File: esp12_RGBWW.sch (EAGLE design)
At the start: 29 parts

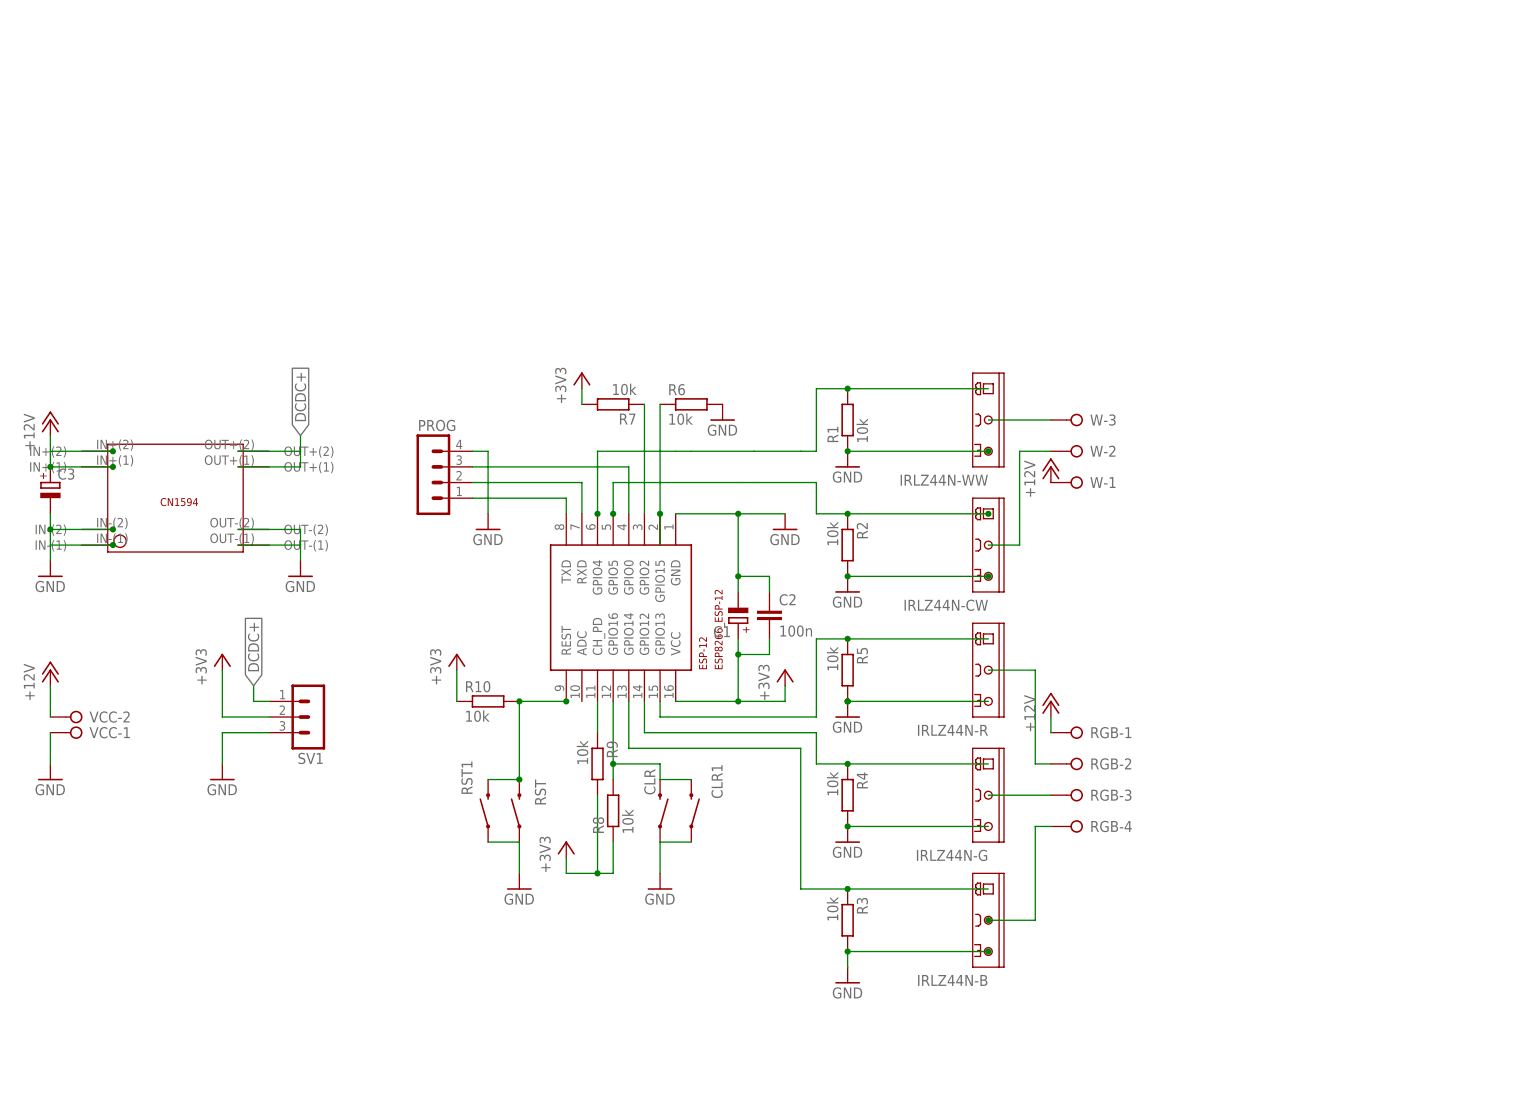
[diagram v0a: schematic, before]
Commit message: new, smaller board
new design, integrated DCDC converter, new, smaller MOSFETs, smaller overal board, additional PRG button, mostly optimized for SMD manufacturing but still hand solderable
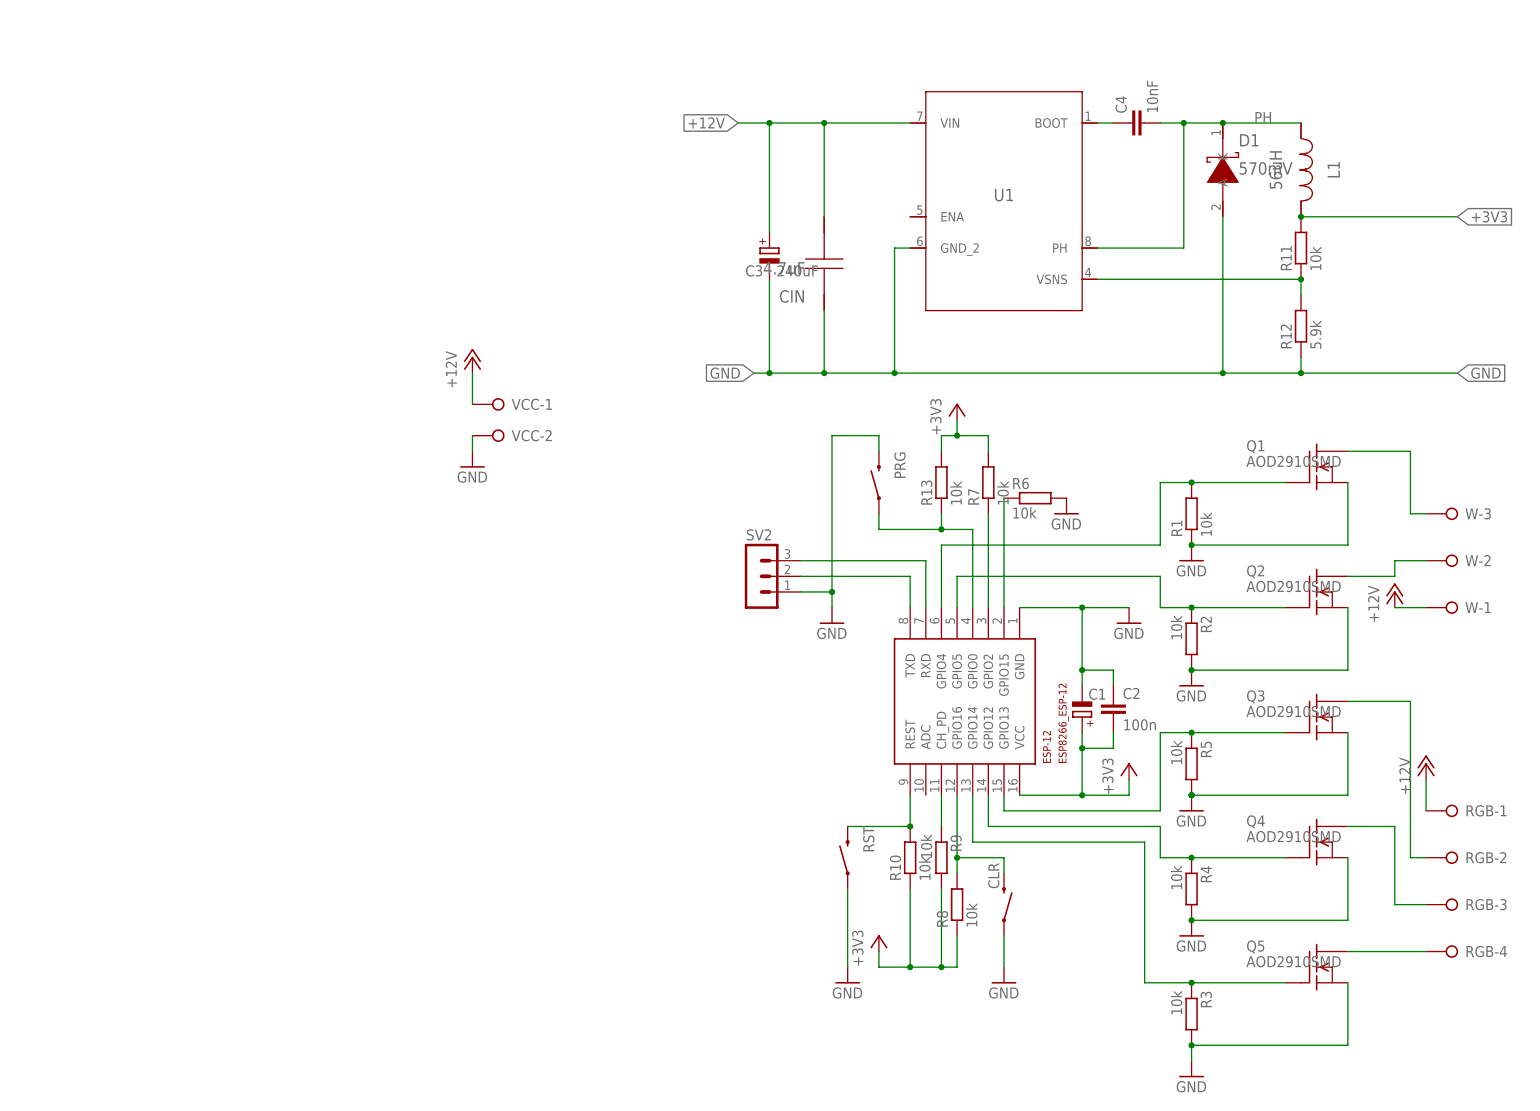
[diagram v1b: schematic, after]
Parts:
- removed CLR1, RST1: SWITCH-MOMENTARY-2SMD-1101NE, SparkFun-Electromechanical:SWITCH-MOMENTARY-2SMD-1101NE
- removed IRLZ44N-B, IRLZ44N-CW, IRLZ44N-G, IRLZ44N-R, IRLZ44N-WW: TIP121, PAsystem:TIP121
- removed PROG: (no value), con-lstb:MA04-1
- removed SV1: (no value), con-lstb:MA03-1
- removed U$2: XM1584, XM1584:XM1584
- added C4: 10nF, resistor:C-EUC0805
- added CIN: 4.7uF, AcceleratedDesigns_Lib:GRM31CR71H475KA12L
- added D1: 570mV, AcceleratedDesigns_Lib:PMEG6010CEH,115
- added L1: 56uH, AcceleratedDesigns_Lib:NPI75C560KTRF
- added PRG: SWITCH-MOMENTARY-2SMD-1101NE, SparkFun-Electromechanical:SWITCH-MOMENTARY-2SMD-1101NE
- added Q1, Q2, Q3, Q4, Q5: AOD2910SMD, transistor-fet+irf7201:AOD2910SMD
- added R11: 10k, resistor:R-EU_R0805
- added R12: 5.9k, resistor:R-EU_R0805
- added R13: 10k, rcl:R-EU_R0805
- added SV2: (no value), con-lstb:MA03-1
- added U1: TPS5410DR, AcceleratedDesigns_Lib:TPS5410DR
- C1: device resistor:CPOL-EUE2.5-6 -> resistor:CPOL-EUE2.5-7
- C3: value (none) -> 240uF; device resistor:CPOL-EUE2.5-6 -> resistor:CPOL-EUE2.5-7
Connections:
- net N$2 renamed CH_PD
- net N$3 renamed G2
- net N$7 renamed G15
- removed net DCDC+: SV1.1, U$2.OUT+(1), U$2.OUT+(2)
- removed net N$1: CLR.2, CLR1.2, ESP-12.GPIO16, R8.2
- removed net N$12: ESP-12.REST, R10.2, RST.2, RST1.2
- removed net N$9: ESP-12.GPIO0, PROG.3
- removed net RGB-B-OUT: IRLZ44N-B.C, RGB-4.KL
- removed net RGB-CW-OUT: IRLZ44N-CW.C, W-2.KL
- removed net RGB-G-OUT: IRLZ44N-G.C, RGB-3.KL
- removed net RGB-R-OUT: IRLZ44N-R.C, RGB-2.KL
- removed net RGB-WW-OUT: IRLZ44N-WW.C, W-3.KL
- new net B: Q5.D, RGB-4.KL
- new net BOOT: C4.1, U1.BOOT
- new net CLR_S: CLR.2, ESP-12.GPIO16, R8.2
- new net CW: Q2.D, W-2.KL
- new net G: Q4.D, RGB-3.KL
- new net PH: C4.2, D1.K, L1.2, U1.PH
- new net PRG_S: ESP-12.GPIO0, PRG.1, R13.1
- new net R: Q3.D, RGB-2.KL
- new net RST_S: ESP-12.REST, R10.2, RST.2
- new net SENS: R11.1, R12.2, U1.VSNS
- new net WW: Q1.D, W-3.KL
- net +12V: now also CIN.2, U1.VIN, VCC-1.KL; no longer U$2.IN+(1), U$2.IN+(2), VCC-2.KL
- net +3V3: now also L1.1, R11.2, R13.2; no longer SV1.2
- net GND: now also CIN.1, D1.A, PRG.2, Q1.S, Q2.S, Q3.S, Q4.S, Q5.S, R12.1, SV2.1, U1.GND_2, VCC-2.KL; no longer CLR1.1, IRLZ44N-B.E, IRLZ44N-CW.E, IRLZ44N-G.E, IRLZ44N-R.E, IRLZ44N-WW.E, PROG.4, RST1.1, SV1.3, U$2.IN-(1), U$2.IN-(2), U$2.OUT-(1), U$2.OUT-(2), VCC-1.KL
- net N$5: now also SV2.3; no longer PROG.2
- net N$8: now also SV2.2; no longer PROG.1
- net RGB-B: now also Q5.G; no longer IRLZ44N-B.B
- net RGB-CW: now also Q2.G; no longer IRLZ44N-CW.B
- net RGB-G: now also Q4.G; no longer IRLZ44N-G.B
- net RGB-R: now also Q3.G; no longer IRLZ44N-R.B
- net RGB-WW: now also Q1.G; no longer IRLZ44N-WW.B
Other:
- moved on the sheet: C1, C2, C3, CLR, ESP-12, R1, R10, R2, R3, R4, R5, R6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

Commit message: minor placement changes
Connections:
- removed net N$5: ESP-12.RXD, SV2.3
- removed net N$8: ESP-12.TXD, SV2.2
- new net RXD: ESP-12.RXD, SV2.2
- new net TXD: ESP-12.TXD, SV2.3
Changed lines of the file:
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@@
 </segment>
 </net>
-<net name="N$5" class="0">
+<net name="RXD" class="0">
 <segment>
 <pinref part="ESP-12" gate="G$1" pin="RXD"/>
-<wire x1="30.48" y1="53.34" x2="30.48" y2="45.72" width="0.1524" layer="91"/>
-<pinref part="SV2" gate="G$1" pin="3"/>
-<wire x1="10.16" y1="53.34" x2="30.48" y2="53.34" width="0.1524" layer="91"/>
+<wire x1="30.48" y1="50.8" x2="30.48" y2="45.72" width="0.1524" layer="91"/>
+<pinref part="SV2" gate="G$1" pin="2"/>
+<wire x1="10.16" y1="50.8" x2="30.48" y2="50.8" width="0.1524" layer="91"/>
 </segment>
 </net>
-<net name="N$8" class="0">
+<net name="TXD" class="0">
 <segment>
 <pinref part="ESP-12" gate="G$1" pin="TXD"/>
-<pinref part="SV2" gate="G$1" pin="2"/>
-<wire x1="10.16" y1="50.8" x2="27.94" y2="50.8" width="0.1524" layer="91"/>
-<wire x1="27.94" y1="50.8" x2="27.94" y2="45.72" width="0.1524" layer="91"/>
+<pinref part="SV2" gate="G$1" pin="3"/>
+<wire x1="10.16" y1="53.34" x2="27.94" y2="53.34" width="0.1524" layer="91"/>
+<wire x1="27.94" y1="53.34" x2="27.94" y2="45.72" width="0.1524" layer="91"/>
 </segment>
 </net>

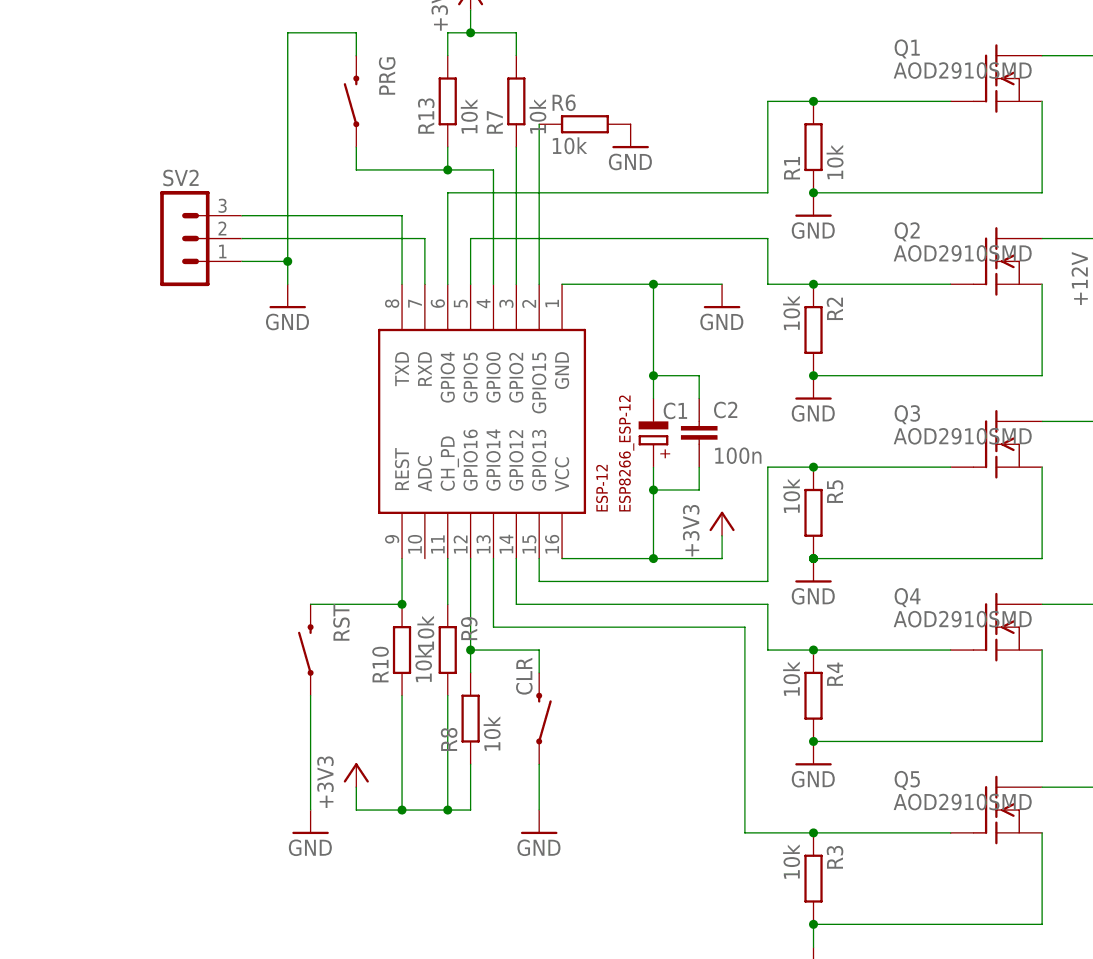
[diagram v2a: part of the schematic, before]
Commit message: updated silk screen
some minor changes, mostly cleaned up silk screen
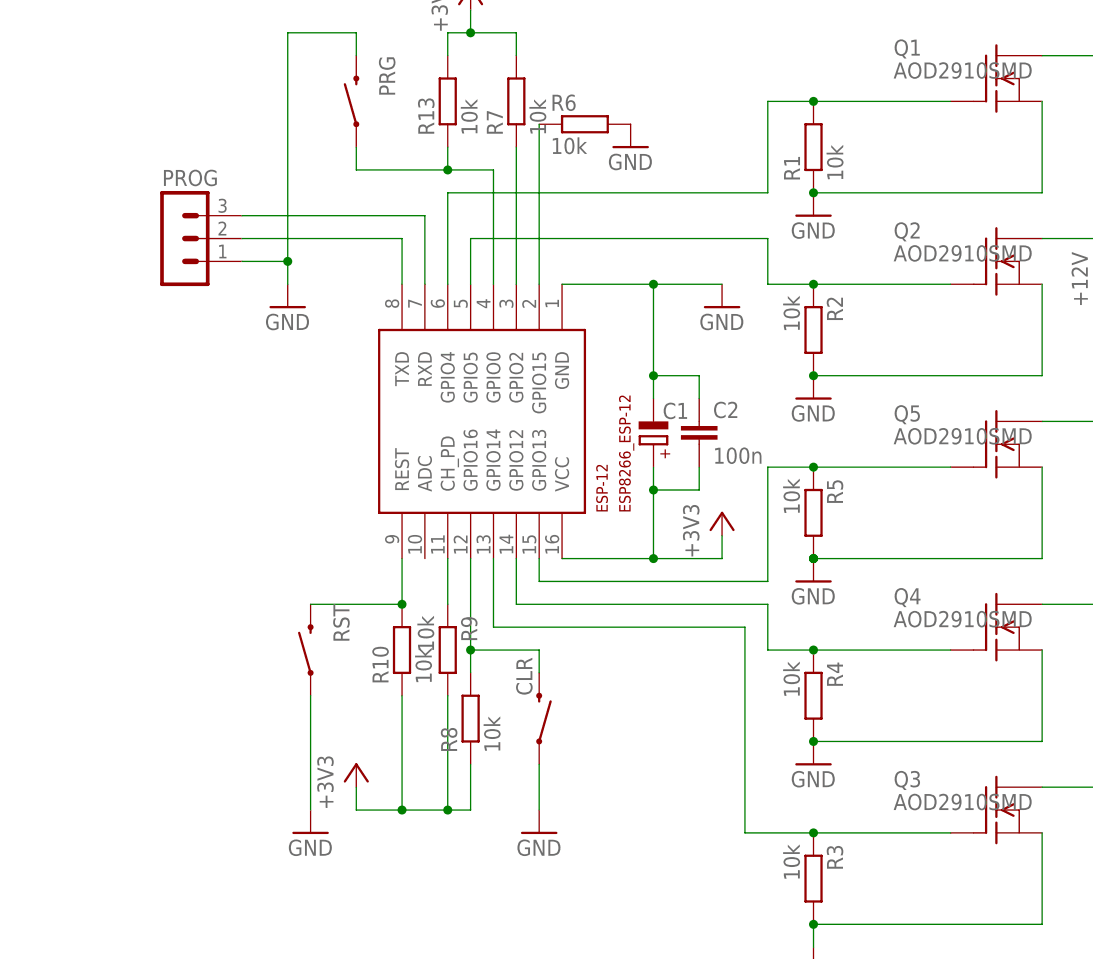
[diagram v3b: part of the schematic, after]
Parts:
- renumbered SV2 to PROG
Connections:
- net B: now also Q3.D; no longer Q5.D
- net R: now also Q5.D; no longer Q3.D
- net RGB-B: now also Q3.G; no longer Q5.G
- net RGB-R: now also Q5.G; no longer Q3.G
- net RXD: now also PROG.3; no longer PROG.2
- net TXD: now also PROG.2; no longer PROG.3
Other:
- moved on the sheet: Q3, Q5
